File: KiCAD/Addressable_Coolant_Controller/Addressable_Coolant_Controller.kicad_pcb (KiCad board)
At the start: 2 copper layers, 210 x 176.5 mm, 84 parts, among them J1 852-002-213R001, J10 XW4M-12D2-H1DA, J11 XW4M-12D2-H1DA, J12 XW4M-02D1-H1DA, J2 852-002-213R001, J3 852-002-213R001, J4 852-002-213R001, J5 852-002-213R001, J6 852-002-213R001, J7 852-002-213R001, J8 852-002-213R001, J9 852-004-213R004, K1 G5V-1, K2 G5V-1, K3 G5V-1, K4 G5V-1, K5 G5V-1, K6 G5V-1, K7 G5V-1, K8 G5V-1, U1 PC12311NSZ1B, U10 ProS3, U2 PC12311NSZ1B, U3 PC12311NSZ1B, U4 PC12311NSZ1B, U5 PC12311NSZ1B, U6 PC12311NSZ1B, U7 PC12311NSZ1B, U8 PC12311NSZ1B, U9 PC12311NSZ1B

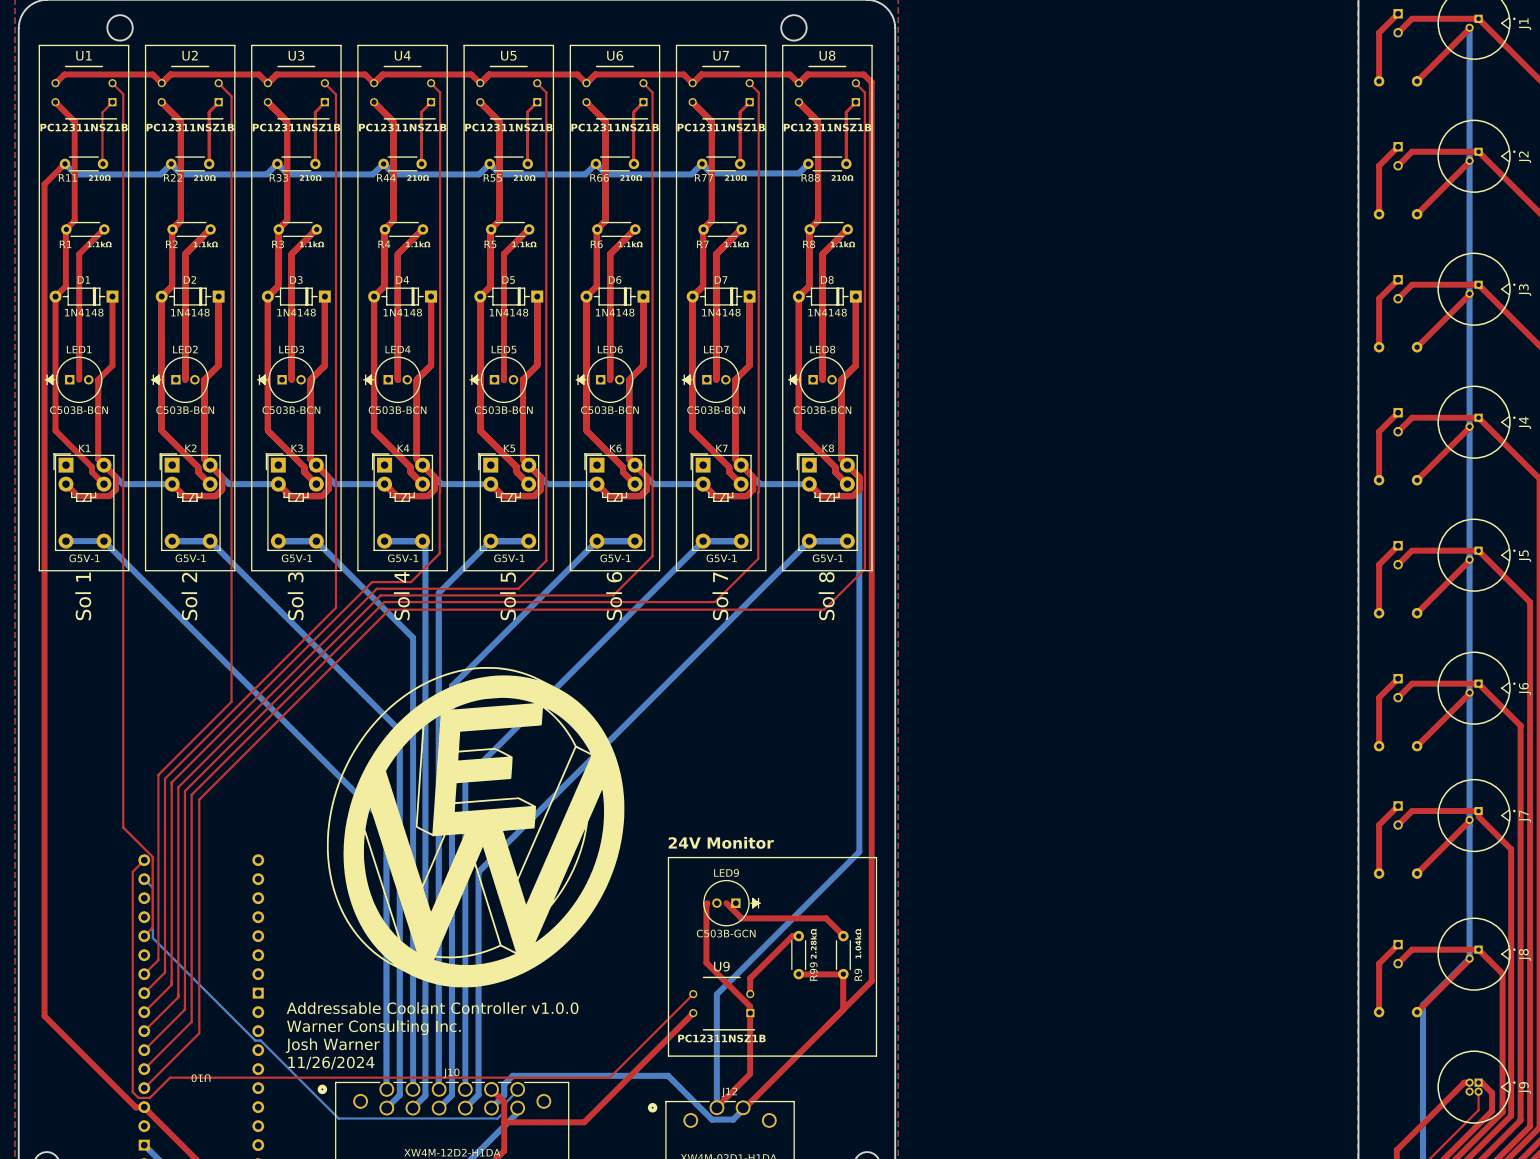
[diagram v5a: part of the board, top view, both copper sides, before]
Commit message: Removing overhanging silkscreen from Omron footprints
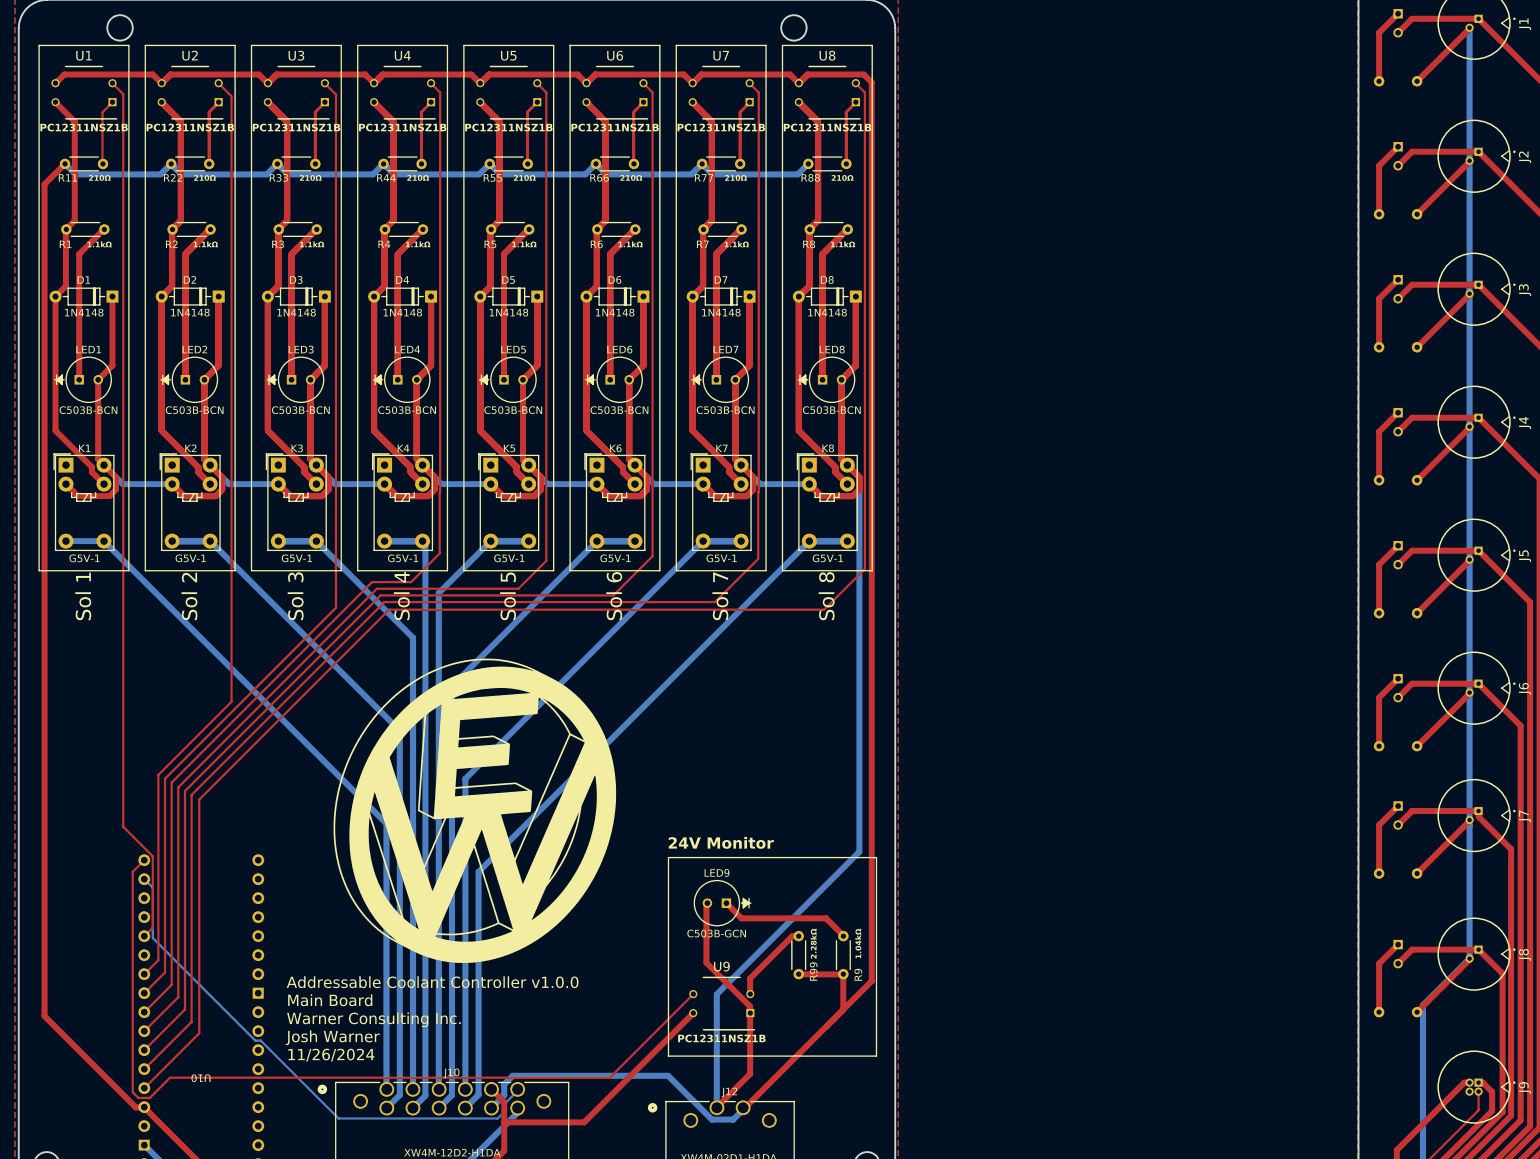
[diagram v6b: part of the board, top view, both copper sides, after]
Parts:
- added G***: LOGO, Warner Consulting Logo:Warner Consulting Logo, B.Cu at (275.2, 145.0)
- moved G*** 2.20 mm to (133.1, 153.0)
- moved LED1 1.27 mm to (81.5, 95.4)
- moved LED5 1.27 mm to (138.3, 95.4)
- moved LED6 1.27 mm to (152.5, 95.4)
- moved LED9 1.27 mm to (165.5, 165.4)
- moved LED2 1.27 mm to (95.7, 95.4)
- moved LED3 1.27 mm to (109.9, 95.4)
- moved LED4 1.27 mm to (124.1, 95.4)
- moved LED7 1.27 mm to (166.7, 95.4)
- moved LED8 1.27 mm to (180.9, 95.4)
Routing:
- net /Main_Board/MCU 3.3v: track 351.0 -> 349.1 mm
- net /Main_Board/IO5: track 144.9 -> 144.2 mm
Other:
- board text added: "Addressable Coolant Controller v1.0.0 Connector Board Warner Consulting Inc. Josh Warner 11/26/2024"
- board text added: "Addressable Coolant Controller v1.0.0 Main Board Warner Consulting Inc. Josh Warner 11/26/2024"
- board text removed: "Addressable Coolant Controller v1.0.0 Warner Consulting Inc. Josh Warner 11/26/2024"

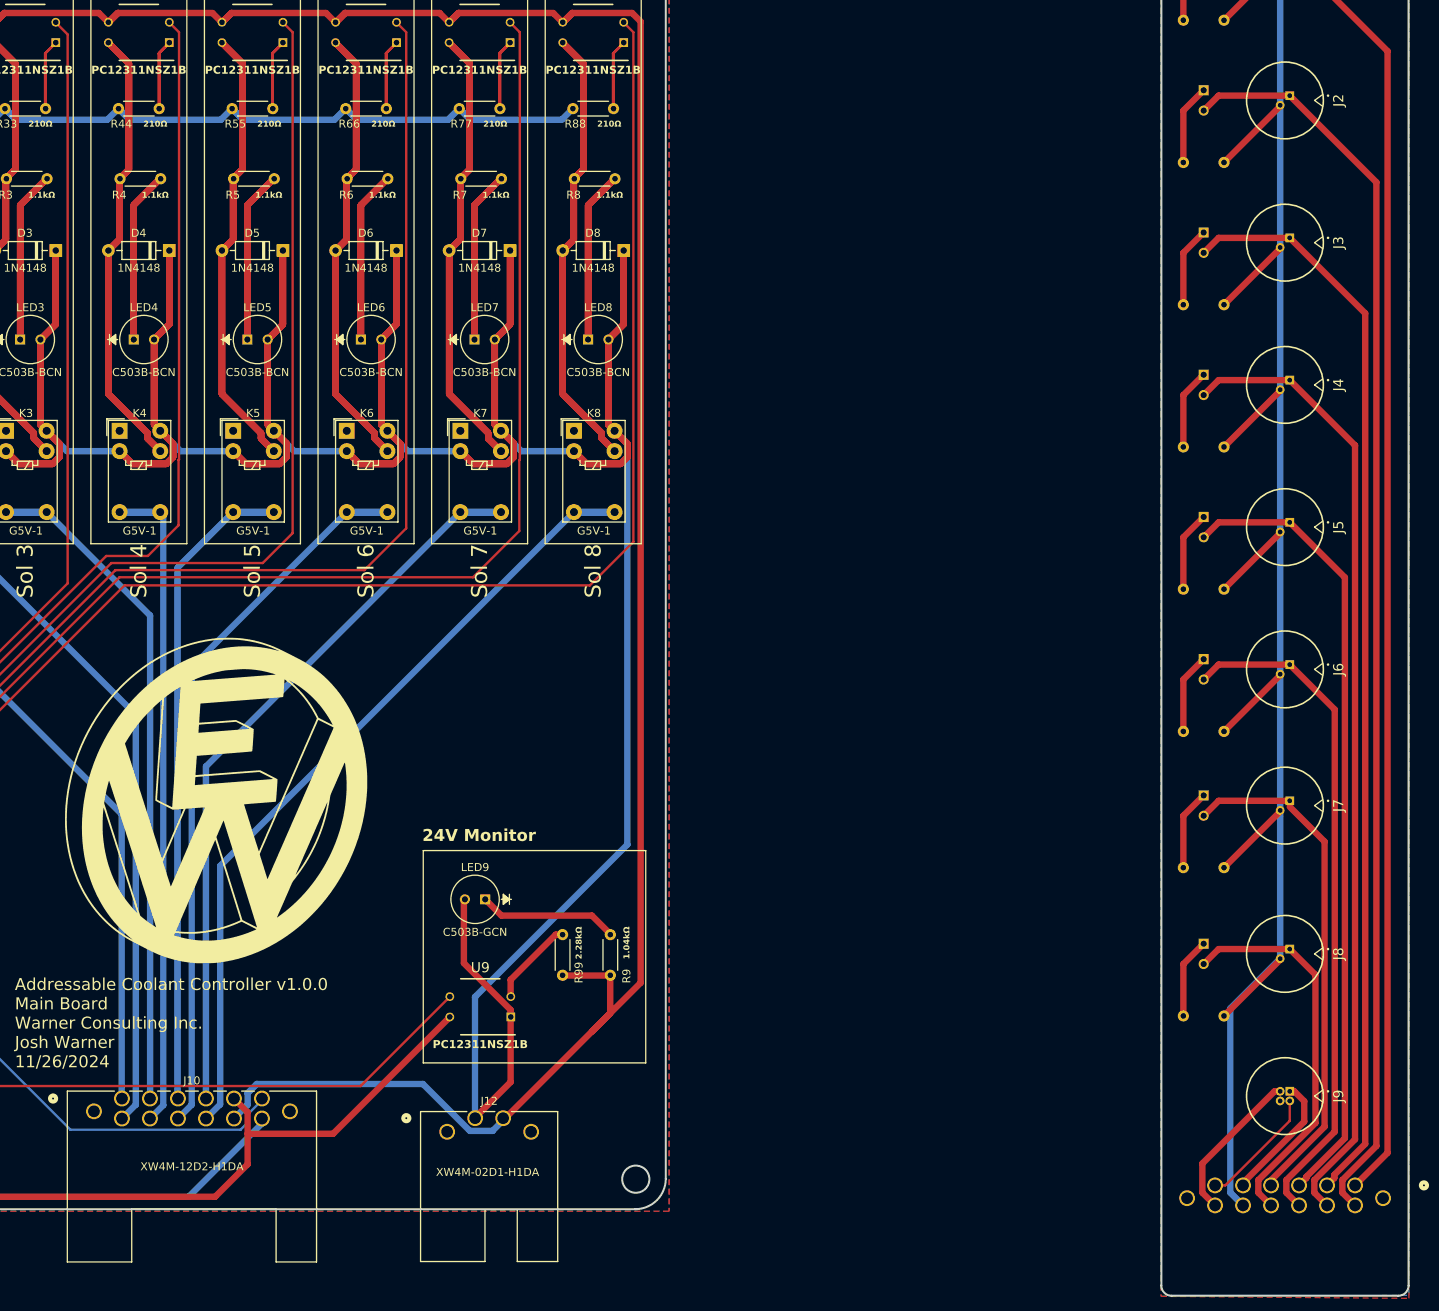
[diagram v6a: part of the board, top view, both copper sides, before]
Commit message: updating 2-pin Omron with square pin 1
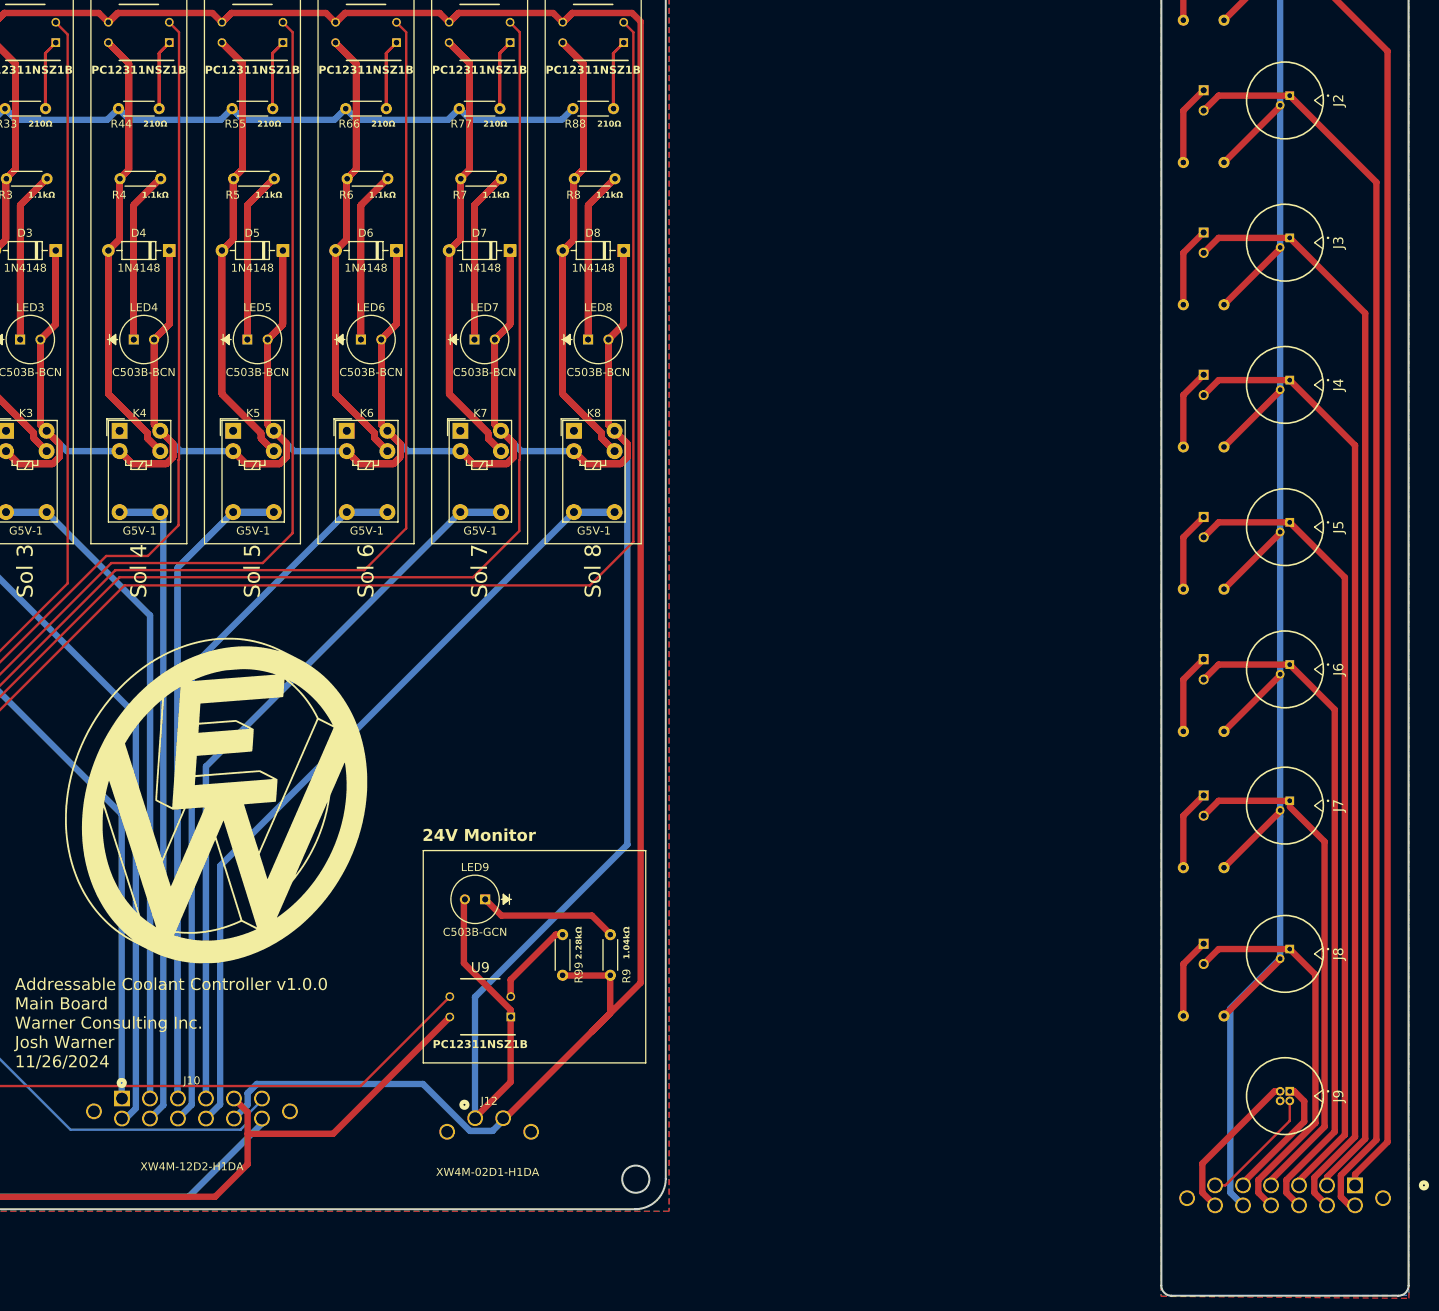
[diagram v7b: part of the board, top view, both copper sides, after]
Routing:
- net /Connector_Board/S2: track 157.2 -> 157.7 mm

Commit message: Finalized board design and exported for ordering
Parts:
- added REF**: KiCad-Logo2_8mm_Copper, Symbol:KiCad-Logo2_8mm_Copper, F.Cu at (169.9, 144.4)
- added REF**: KiCad-Logo2_6mm_Copper, Symbol:KiCad-Logo2_6mm_Copper, B.Cu at (275.4, 128.0)
